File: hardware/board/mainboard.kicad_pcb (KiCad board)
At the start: 4 copper layers, 60 x 110 mm, 266 parts, among them J201 Power, Q601 BCM847, Q701 BCM847, Q801 BCM847, U1 TL074, U2 TL074, U201 TL431A, U3 TL074, U4 TL074, U5 TL074, U6 TL074

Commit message: Slight Changes to Knob Positions
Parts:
- J201: moved to B.Cu
- moved C201 521.1 mm to (-151.6, 254.5)
- moved C202 521.1 mm to (-151.6, 257.5)
- moved C203 521.1 mm to (-151.6, 260.5)
- moved C204 521.1 mm to (-151.6, 263.5)
- moved FB201 521.1 mm to (-160.6, 266.8)
- moved FB202 521.1 mm to (-160.6, 269.3)
- moved D201 521.1 mm to (-151.1, 266.7)
- moved D202 521.1 mm to (-151.1, 270.2)
- moved C205 463.5 mm to (-104.8, 252.9)
- moved R201 463.5 mm to (-100.5, 270.5)
- moved R202 463.5 mm to (-96.2, 252.9)
- moved R203 463.5 mm to (-96.2, 255.4)
- moved R204 463.5 mm to (-96.2, 257.9)
- moved R205 463.5 mm to (-96.2, 260.4)
- moved R206 463.5 mm to (-96.2, 263.0)
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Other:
- board text added: "Cutoff CV"
- board text added: "Filter Core"
- board text added: "Input"
- board text added: "Instability"
- board text added: "LEDs"
- board text added: "Out VCA"
- board text added: "Power In"
- board text added: "Resonance"
- board text added: "VREF"

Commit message: Very first component layout.
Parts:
- moved D923 324.8 mm to (61.7, 66.8), turned to 180 degrees
- moved D921 320.9 mm to (61.7, 69.2), turned to 180 degrees
- moved D919 320.7 mm to (53.1, 76.5), turned to -90 degrees
- moved FB201 318.8 mm to (75.7, 52.7), turned to -90 degrees
- moved FB202 316.8 mm to (78.3, 61.2), turned to 90 degrees
- moved C203 313.8 mm to (83.8, 53.0), turned to 90 degrees
- moved D201 313.4 mm to (78.5, 53.4), turned to 90 degrees
- moved D202 312.8 mm to (82.1, 61.8)
- moved D920 312.0 mm to (56.5, 69.5)
- moved JP701 308.9 mm to (-30.9, 128.4)
- moved JP702 308.9 mm to (-30.9, 132.0)
- moved TP701 308.9 mm to (-34.9, 128.4)
- moved TP702 308.9 mm to (-34.9, 132.0)
- moved C201 308.1 mm to (81.4, 53.0), turned to 90 degrees
- moved D922 305.7 mm to (67.2, 69.2)
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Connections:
- C301 pad 2: Net-(U1C--) -> Net-(U1A--)
- C302 pad 1: Net-(U1D-+) -> Net-(U1B-+)
- C501 pad 2: Net-(U3B--) -> Net-(U3A--)
- C502 pad 2: Net-(U3C--) -> Net-(U3B--)
- C510 pad 2: Net-(U3D--) -> Net-(U3C--)
- C602 pad 2: Net-(U4C--) -> Net-(U4B--)
- C701 pad 1: Net-(U5A-+) -> Net-(U5D-+)
- C704 pad 2: Net-(U5C--) -> Net-(U5A--)
- C705 pad 2: Net-(U5D--) -> Net-(U5B--)
- C801 pad 2: Net-(U2C--) -> Net-(U2D--)
- C802 pad 1: Net-(U2D--) -> Net-(U2A--)
- R202 pad 1: Net-(U1A--) -> Net-(U1C--)
- R204 pad 2: Net-(U1B--) -> Net-(U1D--)
- R205 pad 2: Net-(U1A--) -> Net-(U1C--)
- R206 pad 2: Net-(U1B--) -> Net-(U1D--)
- R302 pad 1: Net-(U1C--) -> Net-(U1A--)
- R303 pad 2: Net-(U1C--) -> Net-(U1A--)
- R305 pad 1: Net-(U1D-+) -> Net-(U1B-+)
- R306 pad 1: Net-(U1D-+) -> Net-(U1B-+)
- R403 pad 1: Net-(U2A--) -> Net-(U2C--)
- R404 pad 2: Net-(U2A--) -> Net-(U2C--)
- R503 pad 1: Net-(U3A-+) -> Net-(U3D-+)
- R505 pad 1: Net-(U3A-+) -> Net-(U3D-+)
- R508 pad 1: Net-(U3B--) -> Net-(U3A--)
- R509 pad 1: Net-(U3B--) -> Net-(U3A--)
- R510 pad 1: Net-(U3C--) -> Net-(U3B--)
- R511 pad 1: Net-(U3C-+) -> Net-(U3B-+)
- R512 pad 2: Net-(U3C-+) -> Net-(U3B-+)
- R513 pad 2: Net-(U3B--) -> Net-(U3A--)
- R514 pad 2: Net-(U3C--) -> Net-(U3B--)
- R517 pad 2: Net-(U3D--) -> Net-(U3C--)
- R518 pad 1: Net-(U3D--) -> Net-(U3C--)
- R604 pad 2: Net-(U4B-+) -> Net-(U4D-+)
- R605 pad 1: Net-(U4B-+) -> Net-(U4D-+)
- R606 pad 1: Net-(U4B--) -> Net-(U4D--)
- R607 pad 2: Net-(U4B--) -> Net-(U4D--)
- R619 pad 1: Net-(U4C--) -> Net-(U4B--)
- R620 pad 1: Net-(U4C-+) -> Net-(U4B-+)
- R621 pad 1: Net-(U4C-+) -> Net-(U4B-+)
- R622 pad 2: Net-(U4C--) -> Net-(U4B--)
- R701 pad 1: Net-(U5A--) -> Net-(U5D--)
- R702 pad 2: Net-(U5A-+) -> Net-(U5D-+)
- R703 pad 2: Net-(U5A--) -> Net-(U5D--)
- R704 pad 1: Net-(U5B--) -> Net-(U5C--)
- R705 pad 2: Net-(U5B--) -> Net-(U5C--)
- R710 pad 1: Net-(U5C--) -> Net-(U5A--)
- R711 pad 1: Net-(U5C--) -> Net-(U5A--)
- R712 pad 2: Net-(U5C--) -> Net-(U5A--)
- R718 pad 1: Net-(U5D--) -> Net-(U5B--)
- R719 pad 1: Net-(U5D-+) -> Net-(U5B-+)
- R720 pad 1: Net-(U5D-+) -> Net-(U5B-+)
- R721 pad 2: Net-(U5D--) -> Net-(U5B--)
- R802 pad 1: Net-(U2C--) -> Net-(U2D--)
- R803 pad 2: Net-(U2C--) -> Net-(U2D--)
- R811 pad 1: Net-(U2D--) -> Net-(U2A--)
- R812 pad 1: Net-(U2D-+) -> Net-(U2A-+)
- R813 pad 1: Net-(U2D-+) -> Net-(U2A-+)
- R814 pad 2: Net-(U2D--) -> Net-(U2A--)
- R901 pad 1: Net-(U4D--) -> Net-(U4C--)
- R902 pad 1: Net-(U4D--) -> Net-(U4C--)
- R903 pad 2: Net-(U4D--) -> Net-(U4C--)
- R907 pad 1: Net-(U6A--) -> Net-(U6C--)
- R908 pad 1: Net-(U6A--) -> Net-(U6C--)
- R909 pad 2: Net-(U6A--) -> Net-(U6C--)
- R913 pad 1: Net-(U6B--) -> Net-(R913-Pad1)
- R914 pad 1: Net-(U6B--) -> Net-(R913-Pad1)
- R915 pad 2: Net-(U6B--) -> Net-(R913-Pad1)
- R927 pad 1: Net-(U6C--) -> Net-(U6B--)
- R928 pad 2: Net-(U6C--) -> Net-(U6B--)
- RV601 pad 2: Net-(U4B-+) -> Net-(U4D-+)
- U1 pad 1: +8VREF -> /Filter Core/LOW_PASS_IN
- U1 pad 10: GND -> /Power/2.5v unbuffered
- U1 pad 12: Net-(U1D-+) -> GND
- U1 pad 13: /Filter Core/HIGH_PASS_IN -> Net-(U1D--)
- U1 pad 14: /Filter Core/HIGH_PASS_IN -> -8VREF
- U1 pad 3: /Power/2.5v unbuffered -> GND
- U1 pad 5: GND -> Net-(U1B-+)
- U1 pad 6: Net-(U1B--) -> /Filter Core/HIGH_PASS_IN
- U1 pad 7: -8VREF -> /Filter Core/HIGH_PASS_IN
- U1 pad 8: /Filter Core/LOW_PASS_IN -> +8VREF
- U2 pad 1: Net-(R404-Pad1) -> Net-(C802-Pad2)
- U2 pad 12: Net-(U2D-+) -> GND
- U2 pad 14: Net-(C802-Pad2) -> Net-(C801-Pad1)
- U2 pad 3: GND -> Net-(U2A-+)
- U2 pad 8: Net-(C801-Pad1) -> Net-(R404-Pad1)
- U3 pad 1: Net-(D502-A) -> Net-(R516-Pad2)
- U3 pad 10: Net-(U3C-+) -> Net-(D506-K)
- U3 pad 12: Net-(D506-K) -> Net-(U3D-+)
- U3 pad 13: Net-(U3D--) -> Net-(D502-A)
- U3 pad 14: Net-(C510-Pad1) -> Net-(D502-A)
- U3 pad 2: Net-(D502-A) -> Net-(U3A--)
- U3 pad 3: Net-(U3A-+) -> GND
- U3 pad 5: GND -> Net-(U3B-+)
- U3 pad 7: Net-(R516-Pad2) -> Net-(D510-K)
- U3 pad 8: Net-(D510-K) -> Net-(C510-Pad1)
- U4 pad 10: Net-(U4C-+) -> GND
- U4 pad 12: GND -> Net-(U4D-+)
- U4 pad 14: Net-(D901-A) -> /Resonance VCA/Resonance_Potentiometer
- U4 pad 7: /Resonance VCA/Resonance_Potentiometer -> /Filter Core/RESONANCE_IN
- U4 pad 8: /Filter Core/RESONANCE_IN -> Net-(D901-A)
- U5 pad 1: Net-(R703-Pad1) -> /Instability VCA/INSTABILITY_CV_OUT
- U5 pad 14: Net-(C705-Pad1) -> Net-(R703-Pad1)
- U5 pad 3: Net-(U5A-+) -> GND
- U5 pad 5: GND -> Net-(U5B-+)
- U5 pad 7: Net-(D701-A) -> Net-(C705-Pad1)
- U5 pad 8: /Instability VCA/INSTABILITY_CV_OUT -> Net-(D701-A)
- U6 pad 1: Net-(D906-A) -> Net-(D911-A)
- U6 pad 2: Net-(U6A--) -> unconnected-(U6A---Pad2)
- U6 pad 7: Net-(D911-A) -> Net-(D925-K)
- U6 pad 8: Net-(D925-K) -> Net-(D906-A)
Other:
- board text removed: "Power In"

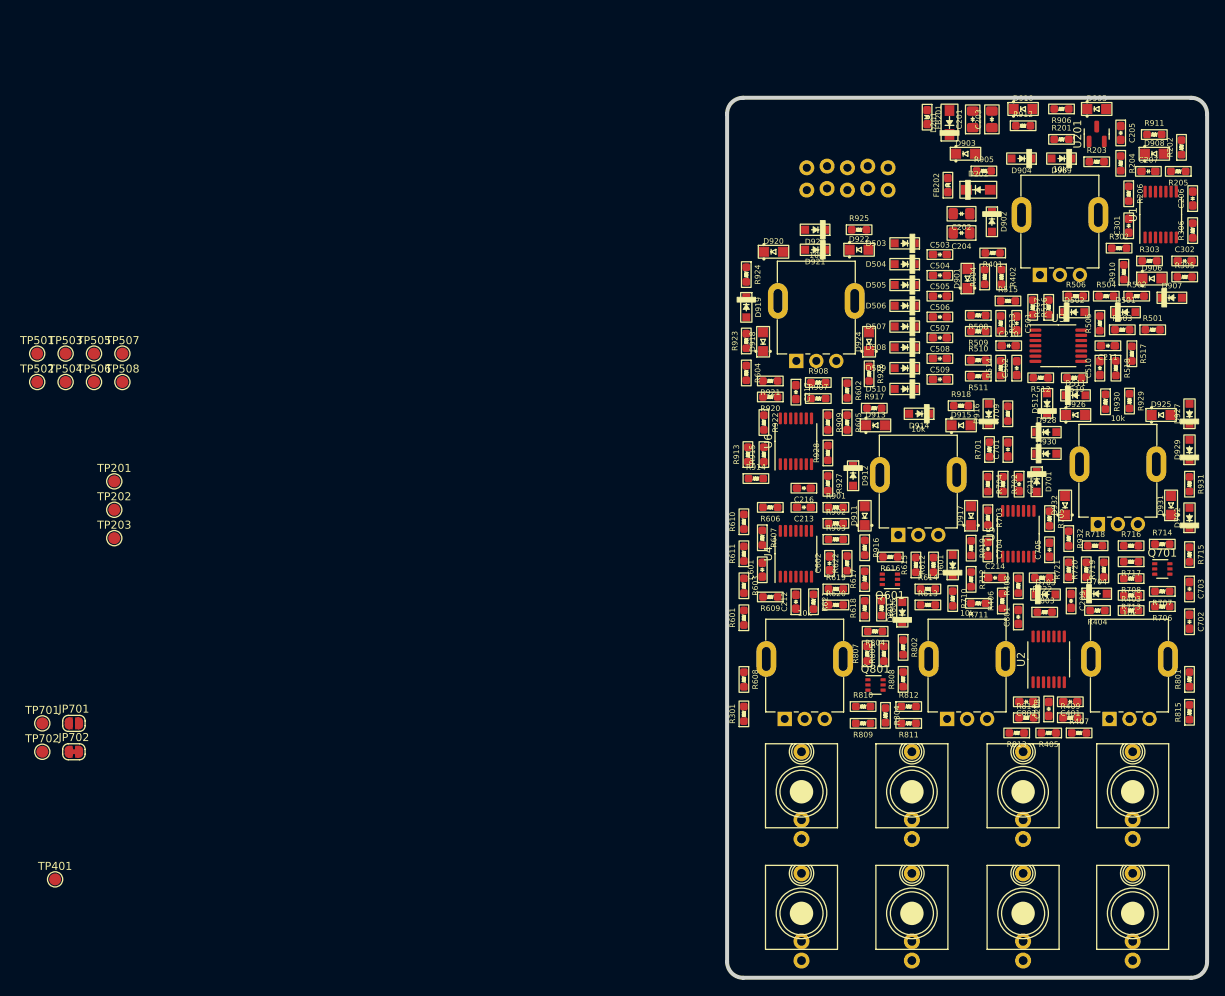
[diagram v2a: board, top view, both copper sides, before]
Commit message: First Draft of layout V2 (All components facing the same way)
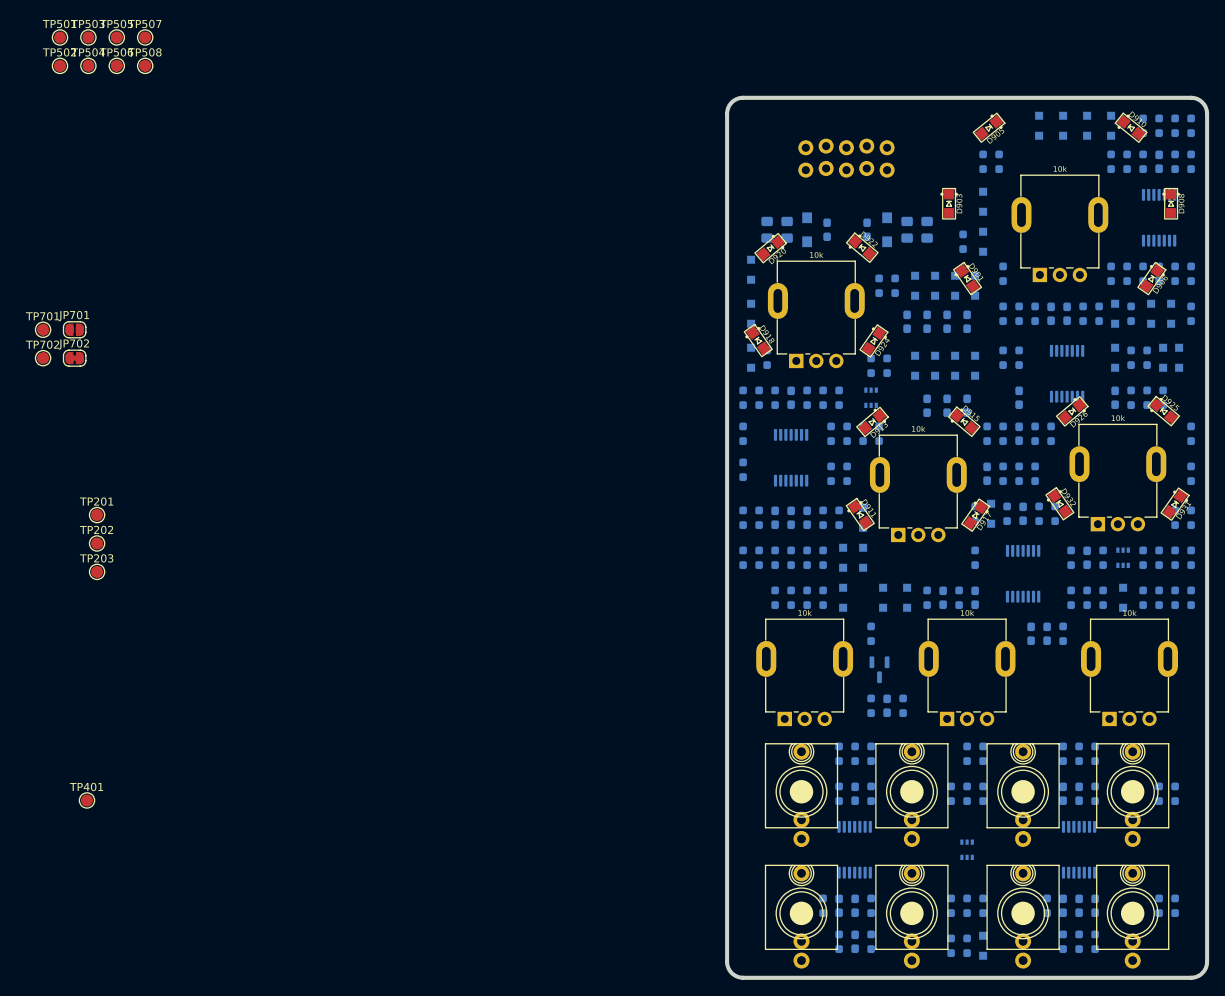
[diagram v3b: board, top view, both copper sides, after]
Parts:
- C201, C202, C203, C204, C205, C206, C207, C208, C209, C210, C211, C212, C213, C214, C215, C216, C217, C301, C302, C401, C501, C502, C503, C504, C505, C506, C507, C508, C509, C510, C601, C602, C701, C702, C703, C704, C705, C801, C802, D201, D202, D501, D502, D503, D504, D505, D506, D507, D508, D509, D510, D511, D512, D601, D701, D702, D703, D704, D801, D902, D904, D907, D909, D912, D914, D916, D919, D921, D923, D927, D928, D929, D930, FB201, FB202, Q601, Q701, Q801, R201, R202, R203, R204, R205, R206, R301, R302, R303, R304, R305, R306, R401, R402, R403, R404, R405, R406, R407, R408, R409, R501, R502, R503, R504, R505, R506, R507, R508, R509, R510, R511, R512, R513, R514, R515, R516, R517, R518, R519, R601, R602, R603, R604, R605, R606, R607, R608, R609, R610, R611, R612, R613, R614, R615, R616, R617, R618, R619, R620, R621, R622, R701, R702, R703, R704, R705, R706, R707, R708, R709, R710, R711, R712, R713, R714, R715, R716, R717, R718, R719, R720, R721, R722, R801, R802, R803, R804, R805, R806, R807, R808, R809, R810, R811, R812, R813, R814, R815, R901, R902, R903, R904, R905, R906, R907, R908, R909, R910, R911, R912, R913, R914, R915, R916, R917, R918, R919, R920, R921, R922, R923, R924, R925, R926, R927, R928, R929, R930, R931, R932, U1, U2, U201, U3, U4, U5, U6: moved to B.Cu
- moved R306 99.3 mm to (64.7, 155.8), turned to -90 degrees
- moved C206 98.8 mm to (64.7, 151.2)
- moved C302 94.5 mm to (66.7, 155.8), turned to -90 degrees
- moved R302 92.1 mm to (68.7, 155.8), turned to -90 degrees
- moved C301 91.6 mm to (66.7, 151.2)
- moved R305 90.7 mm to (62.7, 151.2), turned to -90 degrees
- moved R205 88.6 mm to (64.7, 137.2), turned to -90 degrees
- moved U1 88.1 mm to (66.7, 144.2)
- moved R303 87.8 mm to (68.7, 151.2), turned to -90 degrees
- moved R202 87.0 mm to (64.7, 132.2)
- moved C207 86.0 mm to (66.7, 137.2), turned to 90 degrees
- moved R206 81.6 mm to (68.7, 137.2)
- moved R204 80.1 mm to (68.7, 132.2), turned to 90 degrees
- moved R203 79.9 mm to (66.7, 132.2), turned to -90 degrees
- moved C205 77.3 mm to (70.7, 126.2), turned to 90 degrees
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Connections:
- C401 pad 2: Net-(U2B--) -> Net-(U2A--)
- C501 pad 2: Net-(U3A--) -> Net-(U3C--)
- C510 pad 2: Net-(U3C--) -> Net-(U3A--)
- C601 pad 2: Net-(U4A--) -> Net-(U4B--)
- C602 pad 2: Net-(U4B--) -> Net-(U4A--)
- C801 pad 2: Net-(U2D--) -> Net-(U2C--)
- C802 pad 1: Net-(U2A--) -> Net-(U2B--)
- R403 pad 1: Net-(U2C--) -> Net-(U2D--)
- R404 pad 2: Net-(U2C--) -> Net-(U2D--)
- R405 pad 2: Net-(U2B--) -> Net-(U2A--)
- R406 pad 1: Net-(U2B--) -> Net-(U2A--)
- R407 pad 1: Net-(U2B--) -> Net-(U2A--)
- R408 pad 1: Net-(U2B--) -> Net-(U2A--)
- R409 pad 1: Net-(U2B--) -> Net-(U2A--)
- R508 pad 1: Net-(U3A--) -> Net-(U3C--)
- R509 pad 1: Net-(U3A--) -> Net-(U3C--)
- R513 pad 2: Net-(U3A--) -> Net-(U3C--)
- R517 pad 2: Net-(U3C--) -> Net-(U3A--)
- R518 pad 1: Net-(U3C--) -> Net-(U3A--)
- R604 pad 2: Net-(U4D-+) -> Net-(U4C-+)
- R605 pad 1: Net-(U4D-+) -> Net-(U4C-+)
- R606 pad 1: Net-(U4D--) -> Net-(U4C--)
- R607 pad 2: Net-(U4D--) -> Net-(U4C--)
- R608 pad 1: Net-(U4A--) -> Net-(U4B--)
- R609 pad 1: Net-(U4A--) -> Net-(U4B--)
- R610 pad 1: Net-(U4A--) -> Net-(U4B--)
- R611 pad 2: Net-(U4A--) -> Net-(U4B--)
- R619 pad 1: Net-(U4B--) -> Net-(U4A--)
- R620 pad 1: Net-(U4B-+) -> Net-(U4A-+)
- R621 pad 1: Net-(U4B-+) -> Net-(U4A-+)
- R622 pad 2: Net-(U4B--) -> Net-(U4A--)
- R802 pad 1: Net-(U2D--) -> Net-(U2C--)
- R803 pad 2: Net-(U2D--) -> Net-(U2C--)
- R811 pad 1: Net-(U2A--) -> Net-(U2B--)
- R812 pad 1: Net-(U2A-+) -> Net-(U2B-+)
- R813 pad 1: Net-(U2A-+) -> Net-(U2B-+)
- R814 pad 2: Net-(U2A--) -> Net-(U2B--)
- R901 pad 1: Net-(U4C--) -> Net-(U6A--)
- R902 pad 1: Net-(U4C--) -> Net-(U6A--)
- R903 pad 2: Net-(U4C--) -> Net-(U6A--)
- R913 pad 1: Net-(R913-Pad1) -> Net-(U4D--)
- R914 pad 1: Net-(R913-Pad1) -> Net-(U4D--)
- R915 pad 2: Net-(R913-Pad1) -> Net-(U4D--)
- RV601 pad 2: Net-(U4D-+) -> Net-(U4C-+)
- U2 pad 1: Net-(C802-Pad2) -> /Cutoff CV Driver/CUTOFF_OUT
- U2 pad 14: Net-(C801-Pad1) -> Net-(R404-Pad1)
- U2 pad 3: Net-(U2A-+) -> GND
- U2 pad 5: GND -> Net-(U2B-+)
- U2 pad 7: /Cutoff CV Driver/CUTOFF_OUT -> Net-(C802-Pad2)
- U2 pad 8: Net-(R404-Pad1) -> Net-(C801-Pad1)
- U3 pad 1: Net-(R516-Pad2) -> Net-(C510-Pad1)
- U3 pad 10: Net-(D506-K) -> GND
- U3 pad 3: GND -> Net-(D506-K)
- U3 pad 8: Net-(C510-Pad1) -> Net-(R516-Pad2)
- U4 pad 1: /LED Drivers/RESONANCE_CV_IN -> /Filter Core/RESONANCE_IN
- U4 pad 10: GND -> Net-(U4C-+)
- U4 pad 12: Net-(U4D-+) -> GND
- U4 pad 14: /Resonance VCA/Resonance_Potentiometer -> Net-(D911-A)
- U4 pad 3: GND -> Net-(U4A-+)
- U4 pad 5: Net-(U4B-+) -> GND
- U4 pad 7: /Filter Core/RESONANCE_IN -> /LED Drivers/RESONANCE_CV_IN
- U4 pad 8: Net-(D901-A) -> /Resonance VCA/Resonance_Potentiometer
- U6 pad 1: Net-(D911-A) -> Net-(D901-A)
- U6 pad 2: unconnected-(U6A---Pad2) -> Net-(U6A--)
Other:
- board text added: "Power"

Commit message: Initial Layout Complete
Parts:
- TP201, TP202, TP203, TP401, TP501, TP502, TP503, TP504, TP505, TP506, TP507, TP508, TP701, TP702: moved to B.Cu
- moved TP508 152.7 mm to (107.7, 126.8), turned to 180 degrees
- moved TP501 138.7 mm to (97.2, 91.2), turned to 180 degrees
- moved TP401 136.2 mm to (105.7, 156.2), turned to 180 degrees
- moved TP502 132.0 mm to (55.2, 144.8), turned to 180 degrees
- moved TP504 124.4 mm to (55.2, 137.8), turned to 180 degrees
- moved TP506 117.7 mm to (84.7, 87.2), turned to 180 degrees
- moved TP702 114.4 mm to (79.2, 91.8), turned to 180 degrees
- moved TP505 110.4 mm to (82.2, 66.8), turned to 180 degrees
- moved TP701 109.7 mm to (74.2, 91.8), turned to 180 degrees
- moved TP503 105.6 mm to (70.7, 77.2), turned to 180 degrees
- moved TP507 101.8 mm to (73.7, 77.2), turned to 180 degrees
- moved TP203 95.8 mm to (67.7, 112.2), turned to 180 degrees
- moved TP201 94.8 mm to (65.7, 116.2), turned to 180 degrees
- moved JP701 86.0 mm to (53.0, 98.2)
- moved JP702 86.0 mm to (53.0, 101.8)
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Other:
- board text removed: "Cutoff CV"
- board text removed: "Filter Core"
- board text removed: "Input"
- board text removed: "Instability"
- board text removed: "LEDs"
- board text removed: "Out VCA"
- board text removed: "Power"
- board text removed: "Resonance"
- board text removed: "VREF"

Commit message: Rough Draft of Routing Complete. Ugly but Passes DRC
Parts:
- moved TP702 28.7 mm to (79.5, 120.4)
- moved TP701 25.1 mm to (98.1, 99.3)
- moved C703 17.8 mm to (87.2, 97.2)
- moved R405 15.0 mm to (104.7, 147.2), turned to -90 degrees
- moved R406 15.0 mm to (106.7, 147.2), turned to 90 degrees
- moved D801 10.0 mm to (106.7, 137.2)
- moved R804 10.0 mm to (104.7, 137.2)
- moved R806 10.0 mm to (106.7, 132.2)
- moved D902 7.84 mm to (95.2, 53.7)
- moved D904 7.84 mm to (97.7, 53.7)
- moved R904 7.66 mm to (93.0, 53.8)
- moved D927 7.21 mm to (92.5, 58.8)
- moved R906 6.40 mm to (99.7, 53.8)
- moved R905 5.68 mm to (91.0, 53.8), turned to 90 degrees
- moved D928 5.37 mm to (89.8, 58.8)
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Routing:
- net +12V: track 0.00 -> 287.2 mm, vias 0 -> 9
- net +8VREF: track 0.00 -> 286.4 mm, vias 0 -> 21
- net -8VREF: track 0.00 -> 248.6 mm, vias 0 -> 20
- net -12V: track 0.00 -> 242.7 mm, vias 0 -> 9
- net /Filter Core/OUT: track 0.00 -> 139.2 mm, vias 0 -> 11
- net /Cutoff CV Driver/CUTOFF_OUT: track 0.00 -> 133.7 mm, vias 0 -> 11
- net /LED Drivers/RESONANCE_CV_IN: track 0.00 -> 129.2 mm, vias 0 -> 4
- net /Filter Core/HIGH_PASS_IN: track 0.00 -> 109.0 mm, vias 0 -> 5
- net /Filter Core/LOW_PASS_IN: track 0.00 -> 107.5 mm, vias 0 -> 6
- net Net-(R402-Pad2): track 0.00 -> 94.9 mm, vias 0 -> 4
- net /Cutoff CV Driver/INSTABILITY_IN: track 0.00 -> 89.5 mm, vias 0 -> 6
- net /Cutoff CV Driver/FM1_OUT: track 0.00 -> 88.5 mm, vias 0 -> 2
- net Net-(D918-A): track 0.00 -> 82.8 mm, vias 0 -> 3
- net Net-(D925-K): track 0.00 -> 67.9 mm, vias 0 -> 5
- net GND: track 0.00 -> 62.8 mm, vias 0 -> 66
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- added copper zone on B.Cu, net GND
- added copper zone on F.Cu, net GND
- added copper zone on In1.Cu, net GND
- added copper zone on In2.Cu, net GND

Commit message: Slight routing improvements.
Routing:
- net /LED Drivers/RESONANCE_CV_IN: track 129.2 -> 122.3 mm
- net GND: track 62.8 -> 56.8 mm, vias 66 -> 70
- net Net-(D902-K): track 31.0 -> 28.8 mm
- net /Filter Core/OUT: track 139.2 -> 141.0 mm
- net /Cutoff CV Driver/FM1_OUT: track 88.5 -> 90.2 mm
- net Net-(D916-K): track 16.3 -> 17.8 mm
- net Net-(Q701-C-Pad6): track 16.4 -> 17.9 mm
- net Net-(R404-Pad1): track 52.9 -> 54.3 mm
- net Net-(D914-K): track 37.5 -> 38.7 mm
- net Net-(D912-K): track 37.1 -> 35.9 mm
- net Net-(R703-Pad1): track 19.8 -> 20.8 mm
- net Net-(D904-K): track 17.0 -> 16.1 mm
- net Net-(D918-A): track 82.8 -> 81.9 mm
- net Net-(D502-K): track 43.0 -> 43.8 mm
- net -12V: track 242.7 -> 243.3 mm
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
